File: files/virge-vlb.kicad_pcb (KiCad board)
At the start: 4 copper layers, 240.5 x 70.4 mm, 61 parts, among them J1 VLB_slot, J2 VGA, J3 VESA feature, U1 86C325, U10 74LS245, U2 27C010, Y1 14.318MHz

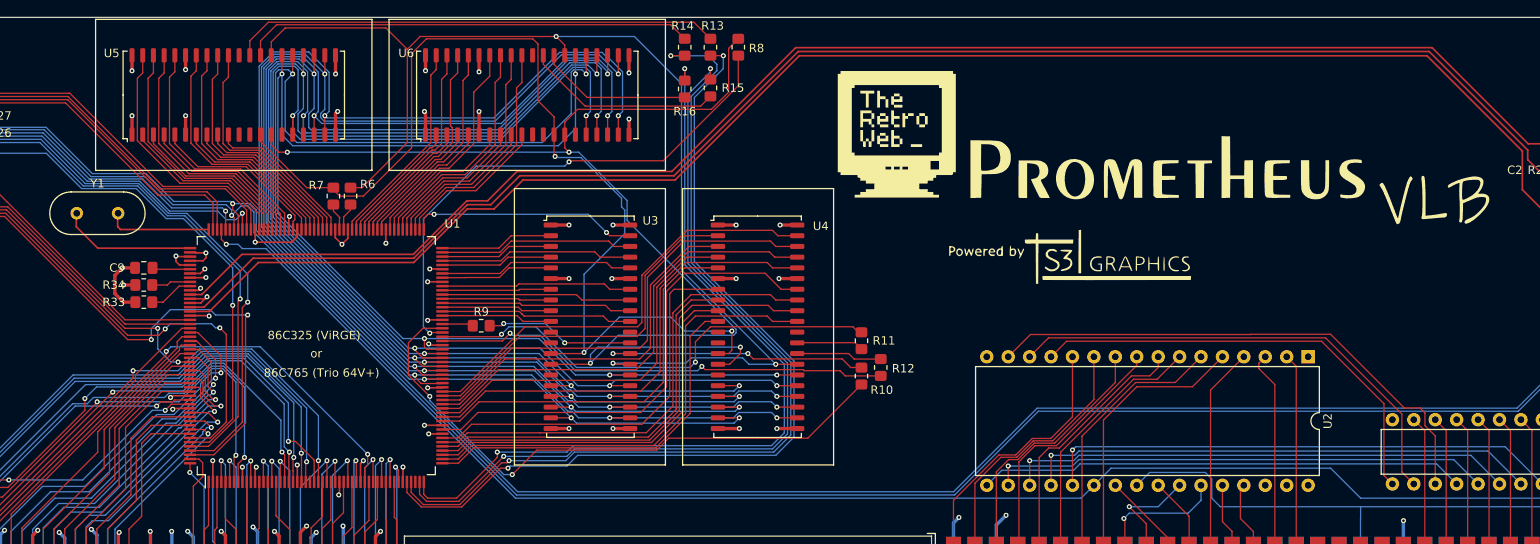
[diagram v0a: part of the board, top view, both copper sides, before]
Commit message: added register strap resistors
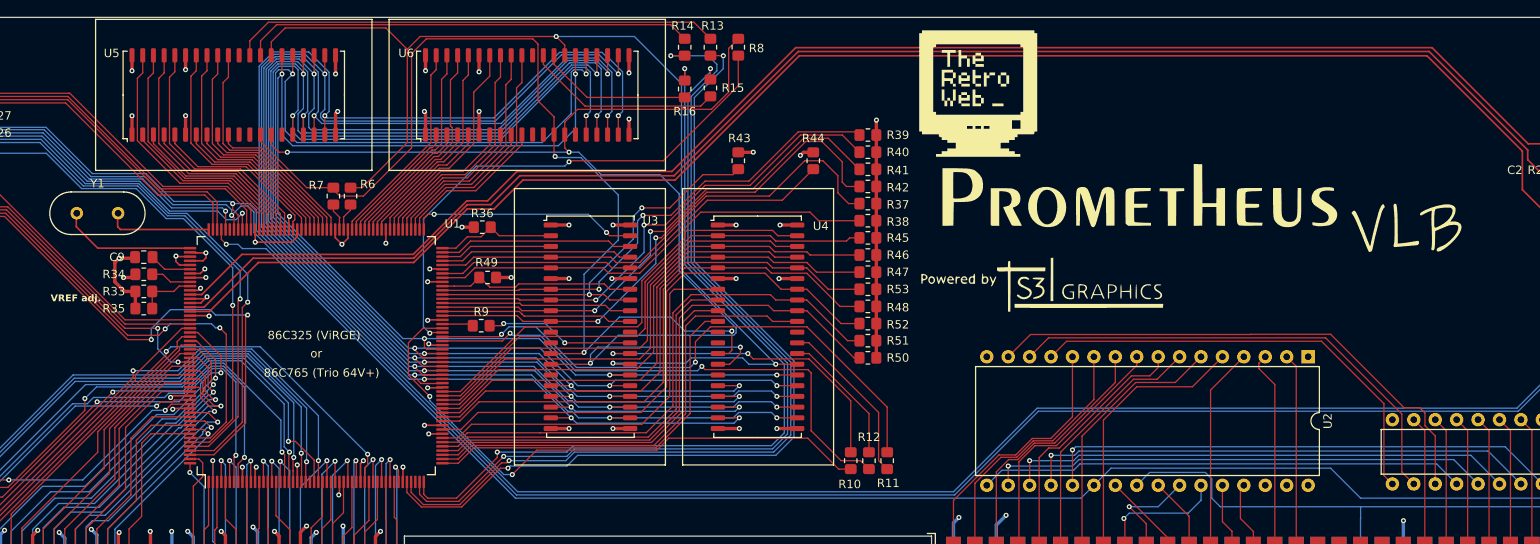
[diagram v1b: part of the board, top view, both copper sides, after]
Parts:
- added R35: ADJ, Resistor_SMD:R_0805_2012Metric_Pad1.20x1.40mm_HandSolder, F.Cu at (88.9, 111.1)
- added R36: 10K, Resistor_SMD:R_0805_2012Metric_Pad1.20x1.40mm_HandSolder, F.Cu at (129.0, 101.5)
- added R37: 10K, Resistor_SMD:R_0805_2012Metric_Pad1.20x1.40mm_HandSolder, F.Cu at (174.8, 98.7)
- added R38: 10K, Resistor_SMD:R_0805_2012Metric_Pad1.20x1.40mm_HandSolder, F.Cu at (174.8, 100.7)
- added R39: 10K, Resistor_SMD:R_0805_2012Metric_Pad1.20x1.40mm_HandSolder, F.Cu at (174.8, 90.6)
- added R40: 10K, Resistor_SMD:R_0805_2012Metric_Pad1.20x1.40mm_HandSolder, F.Cu at (174.8, 92.6)
- added R41: 10K, Resistor_SMD:R_0805_2012Metric_Pad1.20x1.40mm_HandSolder, F.Cu at (174.8, 94.6)
- added R42: 10K, Resistor_SMD:R_0805_2012Metric_Pad1.20x1.40mm_HandSolder, F.Cu at (174.8, 96.6)
- added R43: 10K, Resistor_SMD:R_0805_2012Metric_Pad1.20x1.40mm_HandSolder, F.Cu at (159.4, 93.6)
- added R44: 10K, Resistor_SMD:R_0805_2012Metric_Pad1.20x1.40mm_HandSolder, F.Cu at (168.3, 93.6)
- added R45: 10K, Resistor_SMD:R_0805_2012Metric_Pad1.20x1.40mm_HandSolder, F.Cu at (174.8, 102.7)
- added R46: 10K, Resistor_SMD:R_0805_2012Metric_Pad1.20x1.40mm_HandSolder, F.Cu at (174.8, 104.8)
- added R47: 10K, Resistor_SMD:R_0805_2012Metric_Pad1.20x1.40mm_HandSolder, F.Cu at (174.8, 106.8)
- added R48: 10K, Resistor_SMD:R_0805_2012Metric_Pad1.20x1.40mm_HandSolder, F.Cu at (174.8, 110.9)
- added R49: 10K, Resistor_SMD:R_0805_2012Metric_Pad1.20x1.40mm_HandSolder, F.Cu at (129.7, 107.4)
- added R50: 10K, Resistor_SMD:R_0805_2012Metric_Pad1.20x1.40mm_HandSolder, F.Cu at (174.8, 117.0)
- added R51: 10K, Resistor_SMD:R_0805_2012Metric_Pad1.20x1.40mm_HandSolder, F.Cu at (174.8, 114.9)
- added R52: 10K, Resistor_SMD:R_0805_2012Metric_Pad1.20x1.40mm_HandSolder, F.Cu at (174.8, 112.9)
- added R53: 10K, Resistor_SMD:R_0805_2012Metric_Pad1.20x1.40mm_HandSolder, F.Cu at (174.8, 108.8)
- moved R11 14.5 mm to (177.0, 129.2)
- moved R12 11.1 mm to (174.9, 129.2)
- moved G*** 10.8 mm to (187.8, 85.5)
- moved R10 10.1 mm to (172.7, 129.2)
- moved G*** 4.67 mm to (213.1, 102.7)
- moved C9 1.27 mm to (88.9, 105.0)
- moved R33 1.27 mm to (88.9, 109.1)
- moved R34 1.27 mm to (88.9, 107.1)
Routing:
- net /Memory Bus/PD7: track 13.1 -> 64.0 mm, vias 0 -> 2
- net /Memory Bus/PD6: track 13.0 -> 61.2 mm, vias 0 -> 2
- net /Memory Bus/PD5: track 12.9 -> 60.3 mm, vias 0 -> 2
- net /Memory Bus/PD4: track 12.9 -> 59.5 mm, vias 0 -> 2
- net /Memory Bus/PD2: track 13.2 -> 58.4 mm
- net /Memory Bus/PD3: track 13.3 -> 53.6 mm
- net GND: track 232.3 -> 269.2 mm, vias 48 -> 53
- net /Memory Bus/PD12: track 23.0 -> 49.6 mm
- net /Memory Bus/PD10: track 22.5 -> 48.7 mm, vias 0 -> 2
- net /Memory Bus/PD19: track 46.7 -> 65.3 mm
- net /Memory Bus/PD18: track 45.6 -> 63.1 mm
- net /Memory Bus/PD17: track 44.8 -> 62.0 mm
- net /Memory Bus/PD16: track 44.2 -> 61.0 mm
- net /Memory Bus/CAS2: track 7.94 -> 20.2 mm
- net Net-(U1F-~{CAS2}): track 55.9 -> 67.9 mm
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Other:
- board text added: "VREF adj."

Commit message: initial PCB routed
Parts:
- added C10: 0.1uF, Capacitor_SMD:C_0805_2012Metric_Pad1.18x1.45mm_HandSolder, F.Cu at (142.1, 132.2)
- added C11: 0.1uF, Capacitor_SMD:C_0805_2012Metric_Pad1.18x1.45mm_HandSolder, F.Cu at (161.8, 132.2)
- added C12: 0.1uF, Capacitor_SMD:C_0805_2012Metric_Pad1.18x1.45mm_HandSolder, F.Cu at (153.3, 80.1)
- added C13: 0.1uF, Capacitor_SMD:C_0805_2012Metric_Pad1.18x1.45mm_HandSolder, F.Cu at (80.4, 82.4)
- added C14: 0.1uF, Capacitor_SMD:C_0805_2012Metric_Pad1.18x1.45mm_HandSolder, F.Cu at (244.3, 131.8)
- added C15: 0.1uF, Capacitor_SMD:C_0805_2012Metric_Pad1.18x1.45mm_HandSolder, F.Cu at (62.7, 131.4)
- added R54: 0R, Resistor_SMD:R_0805_2012Metric_Pad1.20x1.40mm_HandSolder, F.Cu at (236.6, 134.2)
- added R55: 0R, Resistor_SMD:R_0805_2012Metric_Pad1.20x1.40mm_HandSolder, F.Cu at (244.5, 120.4)
- U10: footprint Package_DIP:DIP-20_W7.62mm -> Package_SO:SO-20_5.3x12.6mm_P1.27mm
- U2: value 27C010 -> 27C020
- moved R43 15.4 mm to (174.8, 93.7), turned to 180 degrees
- moved U2 13.0 mm to (239.9, 116.5)
- moved U10 8.05 mm to (251.8, 125.5), turned to 180 degrees
- moved G*** 7.98 mm to (221.0, 104.0)
- moved R44 6.75 mm to (174.8, 91.7), turned to 180 degrees
- moved R50 5.46 mm to (174.8, 122.4)
- moved R51 5.33 mm to (174.8, 120.3)
- moved R38 5.21 mm to (174.8, 105.9)
- moved R40 5.21 mm to (174.8, 97.8)
- moved R41 5.21 mm to (174.8, 99.8)
- moved R45 5.21 mm to (174.8, 108.0)
- moved R48 5.21 mm to (174.8, 116.1)
- moved R53 5.21 mm to (174.8, 114.0)
- moved R37 5.21 mm to (174.8, 103.9)
- moved R39 5.21 mm to (174.8, 95.8)
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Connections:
- J1 pad C4: /ISA Bus/IRQ2 -> unconnected-(J1B-IRQ2-PadC4)
- JP2 pad 1: /ISA Bus/IRQ2 -> unconnected-(JP2-Pin_1-Pad1)
- U2 pad 2: /ISA Bus/R_A16 -> Net-(U2-A16)
- U2 pad 30: (no net) -> Net-(U2-A17)
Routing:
- net GND: track 269.2 -> 337.4 mm, vias 53 -> 52
- net VCC: track 110.7 -> 160.7 mm, vias 36 -> 39
- net /ISA Bus/SMEMR: track 78.8 -> 49.0 mm, vias 0 -> 1
- net /ISA Bus/R_A16: track 25.6 -> 0.00 mm
- net /ISA Bus/R_D7: track 61.9 -> 38.9 mm, vias 1 -> 0
- net /Memory Bus/RAS: track 149.3 -> 129.4 mm
- net /ISA Bus/R_D6: track 61.1 -> 41.6 mm, vias 1 -> 0
- net /ISA Bus/R_D5: track 60.3 -> 43.8 mm, vias 1 -> 0
- net /ISA Bus/R_A5: track 32.6 -> 48.3 mm
- net /ISA Bus/R_A8: track 17.8 -> 33.0 mm, vias 1 -> 0
- net /ISA Bus/R_A3: track 32.5 -> 47.5 mm
- net /ISA Bus/R_A7: track 34.9 -> 49.8 mm
- net /ISA Bus/R_A4: track 33.0 -> 47.8 mm
- net /Memory Bus/PD10: track 48.7 -> 63.4 mm
- net /ISA Bus/R_A6: track 33.8 -> 48.2 mm
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
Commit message: added SAUP decoding, adjusted VGA conn.
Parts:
- removed J3: VESA feature, Connector_PinHeader_2.54mm:PinHeader_2x13_P2.54mm_Vertical
- removed JP2: IRQ select, Connector_PinHeader_2.54mm:PinHeader_1x03_P2.54mm_Vertical
- removed R22, R23, R24, R25, R26, R28, R30, R32: 33R, Resistor_SMD:R_0805_2012Metric_Pad1.20x1.40mm_HandSolder
- removed R27, R29, R31: 4K7, Resistor_SMD:R_0805_2012Metric_Pad1.20x1.40mm_HandSolder
- added C16: 0.1uF, Capacitor_SMD:C_0805_2012Metric_Pad1.18x1.45mm_HandSolder, F.Cu at (88.4, 115.4)
- added C17: 0.1uF, Capacitor_SMD:C_0805_2012Metric_Pad1.18x1.45mm_HandSolder, F.Cu at (84.1, 115.4)
- added C18: 0.1uF, Capacitor_SMD:C_0805_2012Metric_Pad1.18x1.45mm_HandSolder, F.Cu at (86.2, 115.4)
- added U7: 74LS244, Package_SO:SO-20_5.3x12.6mm_P1.27mm, F.Cu at (253.6, 125.5)
- added U8: 4052, Package_SO:SO-16_3.9x9.9mm_P1.27mm, F.Cu at (77.6, 113.5)
- added U9: 74HC04, Package_SO:SO-14_3.9x8.65mm_P1.27mm, F.Cu at (59.4, 118.0)
- R18, R19, R20: value 33R -> 10K
- R21: value 33R -> 4K7
- U10: value 74LS245 -> 7408; footprint Package_SO:SO-20_5.3x12.6mm_P1.27mm -> Package_SO:SO-14_3.9x8.65mm_P1.27mm
- moved U10 193.1 mm to (59.4, 109.1), turned to 90 degrees
- moved R18 33.9 mm to (73.4, 108.0), turned to 0 degrees
- moved R19 32.0 mm to (66.8, 111.6), turned to 90 degrees
- moved R20 30.6 mm to (69.0, 111.6), turned to -90 degrees
- moved R21 29.4 mm to (71.1, 111.6), turned to -90 degrees
- moved C3 11.7 mm to (258.8, 87.4), turned to 0 degrees
- moved C1 11.3 mm to (267.0, 87.4), turned to 0 degrees
- moved C7 11.1 mm to (267.2, 119.9)
- moved C8 11.1 mm to (267.2, 117.3)
- moved R4 11.1 mm to (267.2, 122.0)
- moved R5 11.1 mm to (267.2, 115.2)
- moved C2 9.92 mm to (263.0, 87.4), turned to 0 degrees
- moved R3 9.11 mm to (258.8, 89.7), turned to 0 degrees
- moved R1 8.64 mm to (267.0, 89.7), turned to 0 degrees
- moved J2 8.21 mm to (274.7, 101.2)
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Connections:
- J1 pad A22: /VL Bus/VL_A28 -> unconnected-(J1A-A28-PadA22)
- J1 pad A54: /VL Bus/ID2 -> unconnected-(J1A-ID2-PadA54)
- J1 pad A55: /VL Bus/ID3 -> unconnected-(J1A-ID3-PadA55)
- J1 pad A56: /VL Bus/ID4 -> unconnected-(J1A-ID4-PadA56)
- J1 pad B21: /VL Bus/VL_A31 -> unconnected-(J1A-A31-PadB21)
- J1 pad B24: /VL Bus/VL_A27 -> unconnected-(J1A-A27-PadB24)
- J1 pad B53: /VL Bus/ID0 -> unconnected-(J1A-ID0-PadB53)
- J1 pad B54: /VL Bus/ID1 -> unconnected-(J1A-ID1-PadB54)
- J1 pad C46: /ISA Bus/R_A16 -> unconnected-(J1B-BA16-PadC46)
- J2 pad 12: unconnected-(J2-Pad12) -> Net-(U8-Y3)
- J2 pad 15: unconnected-(J2-Pad15) -> Net-(U8-X3)
- R18 pad 1: Net-(U1D-LD0/PA0) -> VCC
- R19 pad 1: Net-(U1D-LD1/PA1) -> Net-(U8-Y1)
- R19 pad 2: Net-(J3-Pin_4) -> VCC
- R20 pad 1: Net-(U1D-LD2/PA2) -> VCC
- R20 pad 2: Net-(J3-Pin_6) -> Net-(U8-Y3)
- R21 pad 1: Net-(U1D-LD3/PA3) -> VCC
- R21 pad 2: Net-(J3-Pin_8) -> Net-(U8-X3)
- U1 pad 146: Net-(U1D-LD0/PA0) -> unconnected-(U1D-LD0/PA0-Pad146)
- U1 pad 147: Net-(U1D-LD1/PA1) -> unconnected-(U1D-LD1/PA1-Pad147)
- U1 pad 148: /LCLK -> unconnected-(U1H-LCLK/VCLK-Pad148)
- U1 pad 151: unconnected-(U1H-~{GPIOSTR}/~{ENFEAT}/GOP0-Pad151) -> /ENFEAT
- U1 pad 152: /VL Bus/SINTR -> /VL Bus/IRQ9
- U1 pad 154: Net-(U1D-LD2/PA2) -> unconnected-(U1D-LD2/PA2-Pad154)
- U1 pad 155: Net-(U1D-LD3/PA3) -> unconnected-(U1D-LD3/PA3-Pad155)
- U1 pad 174: Net-(U1D-LD4/PA4) -> unconnected-(U1D-LD4/PA4-Pad174)
- U1 pad 175: Net-(U1D-LD5/PA5) -> unconnected-(U1D-LD5/PA5-Pad175)
- U1 pad 184: Net-(U1D-LD6/PA6) -> unconnected-(U1D-LD6/PA6-Pad184)
- U1 pad 202: Net-(U1D-LD7/PA7) -> unconnected-(U1D-LD7/PA7-Pad202)
- U1 pad 203: /EVIDEO -> unconnected-(U1H-~{VREQ}/VRDY/EVIDEO-Pad203)
- U1 pad 204: /EVCLK -> unconnected-(U1H-~{CREQ}/CRDY/EVCLK-Pad204)
- U1 pad 205: /ESYNC -> /SPCLK
- U1 pad 206: /BLANK -> /SPD
- U1 pad 25: unconnected-(U1H-SAUP1-Pad25) -> /VL Bus/SAUP1
- U1 pad 50: unconnected-(U1H-SAUP2-Pad50) -> /VL Bus/VL_A30
- U10 pad 1: /ISA Bus/SMEMR -> Net-(U10-Pad1)
- U10 pad 10: GND -> Net-(U10-Pad10)
- U10 pad 11: /ISA Bus/R_D0 -> /VL Bus/SAUP1
- U10 pad 12: /ISA Bus/R_D1 -> Net-(U10-Pad12)
- U10 pad 13: /ISA Bus/R_D2 -> Net-(U10-Pad13)
- U10 pad 14: /ISA Bus/R_D3 -> VCC
- U10 pad 2: /ISA Bus/ISA_D7 -> Net-(U10-Pad2)
- U10 pad 3: /ISA Bus/ISA_D6 -> Net-(U10-Pad3)
- U10 pad 4: /ISA Bus/ISA_D5 -> Net-(U10-Pad4)
- U10 pad 5: /ISA Bus/ISA_D4 -> Net-(U10-Pad5)
- U10 pad 6: /ISA Bus/ISA_D3 -> Net-(U10-Pad10)
- U10 pad 7: /ISA Bus/ISA_D2 -> GND
- U10 pad 8: /ISA Bus/ISA_D1 -> Net-(U10-Pad12)
- U10 pad 9: /ISA Bus/ISA_D0 -> Net-(U10-Pad3)
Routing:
- net Net-(U8-Y3): track 0.00 -> 288.1 mm, vias 0 -> 1
- net Net-(U8-X3): track 0.00 -> 268.8 mm, vias 0 -> 1
- net GND: track 337.4 -> 176.2 mm, vias 52 -> 53
- net /VL Bus/VL_A23: track 0.00 -> 90.4 mm, vias 0 -> 3
- net /VL Bus/VL_A24: track 0.00 -> 89.2 mm, vias 0 -> 4
- net /VL Bus/VL_A29: track 0.00 -> 88.5 mm, vias 0 -> 3
- net /VL Bus/VL_A26: track 0.00 -> 86.6 mm, vias 0 -> 4
- net /VL Bus/VL_A25: track 0.00 -> 85.5 mm, vias 0 -> 3
- net /BLANK: track 85.3 -> 0.00 mm, vias 2 -> 0
- net /EVCLK: track 80.3 -> 0.00 mm, vias 2 -> 0
- net /VL Bus/SINTR: track 74.1 -> 0.00 mm, vias 1 -> 0
- net /VL Bus/SAUP1: track 0.00 -> 73.5 mm, vias 0 -> 2
- net /ESYNC: track 69.9 -> 0.00 mm, vias 2 -> 0
- net /VS: track 260.9 -> 194.3 mm
- net Net-(U1D-LD7/PA7): track 65.9 -> 0.00 mm, vias 2 -> 0
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- added copper zone on F.Cu, net GND
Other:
- board text added: "74LS244"
- board text added: "Bank 0"
- board text added: "Bank 1"
- board text added: "S3 chip goes here lol"
- board text added: "Video BIOS"
- board text removed: "86C325 (ViRGE)"
- board text removed: "86C765 (Trio 64V+)"
- board text removed: "or"

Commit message: added ground vias, polished silkscreen
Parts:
- C10, C11, C12, C13, C14, C15, C9: value 0.1uF -> 100nF
- C17: value 0.1uF -> 3 x 100nF
- C3, C6: value 10pF -> 3 x 10pF
- R10, R13: value 33R -> 3 x 33R
- R16, R6: value 33R -> 2 x 33R
- R3: value 75R -> 3 x 75R
- R44: value 10K -> 10K each
- R54, R55: value 0R -> 0
- U9: value 74HC04 -> 7404
- moved R18 0.90 mm to (74.3, 108.1)
- moved C7 0.27 mm to (267.0, 119.9)
- moved R4 0.25 mm to (267.0, 122.0)
- moved C8 0.24 mm to (267.0, 117.3)
- moved R5 0.24 mm to (267.0, 115.2)
- renumbered J2 to VGA
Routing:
- net GND: track 176.2 -> 171.7 mm, vias 53 -> 160
- net VCC: track 171.7 -> 174.0 mm
- net /VL Bus/SAUP1: track 73.5 -> 72.3 mm
- added copper zone on B.Cu, net GND
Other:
- board text added: "Config section"
- board text added: "Very Long Bus"
- board text added: "more Config"

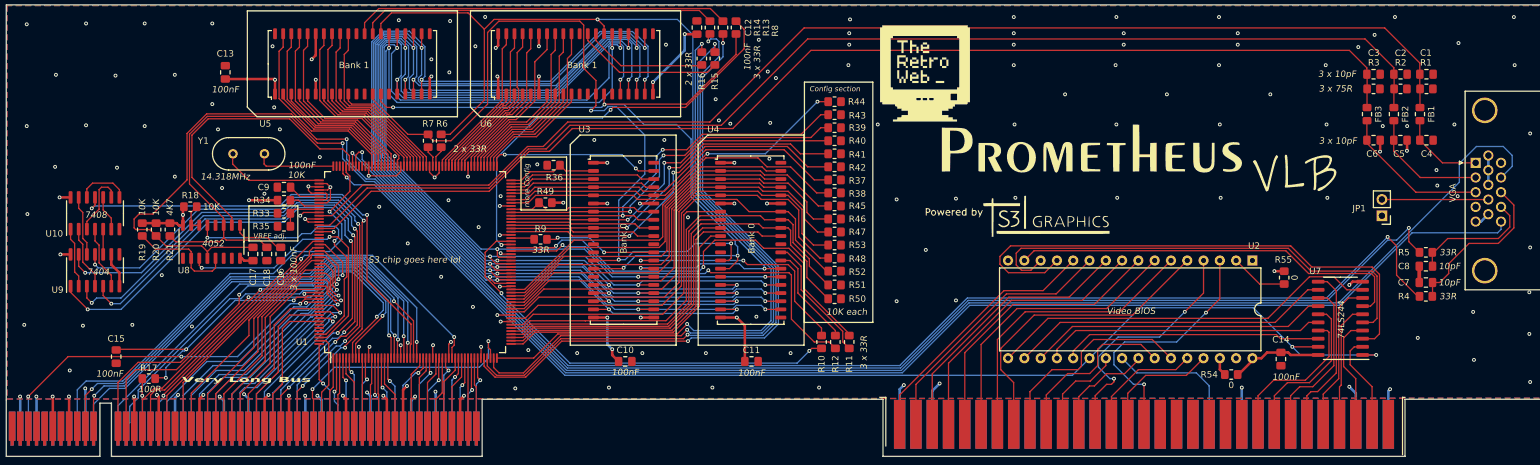
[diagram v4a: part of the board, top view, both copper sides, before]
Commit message: added address jumpers
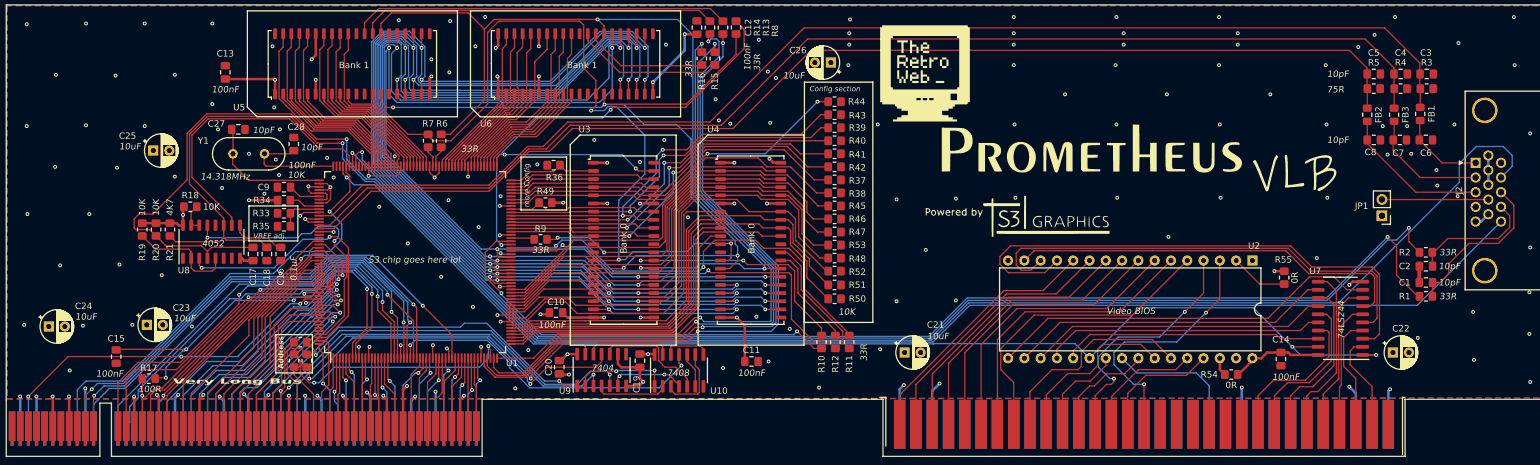
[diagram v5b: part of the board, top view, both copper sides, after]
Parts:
- removed VGA: VGA, Connector_Dsub:DSUB-15-HD_Female_Horizontal_P2.29x1.98mm_EdgePinOffset8.35mm_Housed_MountingHolesOffset10.89mm
- added C10: 100nF, Capacitor_SMD:C_0805_2012Metric_Pad1.18x1.45mm_HandSolder, F.Cu at (131.3, 124.6)
- added C20: 100nF, Capacitor_SMD:C_0805_2012Metric_Pad1.18x1.45mm_HandSolder, F.Cu at (131.8, 133.1)
- added C21: 10uF, Capacitor_THT:CP_Radial_D5.0mm_P2.50mm, F.Cu at (185.7, 130.8)
- added C22: 10uF, Capacitor_THT:CP_Radial_D5.0mm_P2.50mm, F.Cu at (261.8, 130.8)
- added C23: 10uF, Capacitor_THT:CP_Radial_D5.0mm_P2.50mm, F.Cu at (67.5, 126.5)
- added C24: 10uF, Capacitor_THT:CP_Radial_D5.0mm_P2.50mm, F.Cu at (52.2, 126.7)
- added C25: 10uF, Capacitor_THT:CP_Radial_D5.0mm_P2.50mm, F.Cu at (68.5, 99.3)
- added C26: 10uF, Capacitor_THT:CP_Radial_D5.0mm_P2.50mm, F.Cu at (174.2, 85.6)
- added C27: 10pF, Capacitor_SMD:C_0805_2012Metric_Pad1.18x1.45mm_HandSolder, F.Cu at (81.8, 96.0)
- added C28: 10pF, Capacitor_SMD:C_0805_2012Metric_Pad1.18x1.45mm_HandSolder, F.Cu at (90.4, 98.3)
- added J2: VGA, Connector_Dsub:DSUB-15-HD_Female_Horizontal_P2.29x1.98mm_EdgePinOffset8.35mm_Housed_MountingHolesOffset10.89mm, F.Cu at (274.7, 101.2)
- added R22: 0, Resistor_SMD:R_0805_2012Metric_Pad1.20x1.40mm_HandSolder, F.Cu at (91.4, 129.2)
- added R23: 0, Resistor_SMD:R_0805_2012Metric_Pad1.20x1.40mm_HandSolder, F.Cu at (92.5, 132.1)
- added R24: 0, Resistor_SMD:R_0805_2012Metric_Pad1.20x1.40mm_HandSolder, F.Cu at (90.5, 132.1)
- C17: value 3 x 100nF -> 0.1uF
- C3, C6: value 3 x 10pF -> 10pF
- R1, R2: value 75R -> 33R
- R10, R13: value 3 x 33R -> 33R
- R16, R6: value 2 x 33R -> 33R
- R3: value 3 x 75R -> 75R
- R4, R5: value 33R -> 75R
- R44: value 10K each -> 10K
- R54, R55: value 0 -> 0R
- moved U10 94.3 mm to (150.5, 133.6)
- moved U9 80.5 mm to (138.4, 133.5)
- moved R4 32.6 mm to (263.0, 89.7)
- moved C1 32.5 mm to (267.0, 119.9), turned to 180 degrees
- moved R1 32.3 mm to (267.0, 122.0)
- moved C2 30.2 mm to (267.0, 117.3), turned to 180 degrees
- moved R5 26.8 mm to (258.8, 89.7)
- moved R2 25.8 mm to (267.0, 115.2)
- moved C7 22.6 mm to (262.9, 97.7)
- moved C8 21.3 mm to (258.8, 97.7)
- moved C5 11.1 mm to (258.8, 87.4)
- moved C4 11.1 mm to (263.0, 87.4)
- moved C3 8.29 mm to (267.1, 87.4)
- moved R3 8.29 mm to (267.1, 89.7)
- moved C6 8.17 mm to (267.0, 97.7)
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- renumbered C10 to C19
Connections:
- net Net-(U8-X3) renamed /DDC_SCL
- net Net-(U8-Y3) renamed /DDC_SDA
- C1 pad 1: /S3_RED -> Net-(C1-Pad1)
- C2 pad 1: /S3_GREEN -> Net-(C2-Pad1)
- C3 pad 1: /S3_BLUE -> /S3_RED
- C4 pad 1: /RED -> /S3_GREEN
- C5 pad 1: /GREEN -> /S3_BLUE
- C6 pad 1: /BLUE -> /RED
- C7 pad 1: GND -> /GREEN
- C7 pad 2: /HSYNC -> GND
- C8 pad 1: GND -> /BLUE
- C8 pad 2: /VSYNC -> GND
- FB2 pad 1: /GREEN -> /BLUE
- FB2 pad 2: /S3_GREEN -> /S3_BLUE
- FB3 pad 1: /BLUE -> /GREEN
- FB3 pad 2: /S3_BLUE -> /S3_GREEN
- R1 pad 1: /S3_RED -> /HS
- R1 pad 2: GND -> Net-(C1-Pad1)
- R2 pad 1: /S3_GREEN -> /VS
- R2 pad 2: GND -> Net-(C2-Pad1)
- R3 pad 1: /S3_BLUE -> /S3_RED
- R4 pad 1: /HS -> /S3_GREEN
- R4 pad 2: /HSYNC -> GND
- R5 pad 1: /VS -> /S3_BLUE
- R5 pad 2: /VSYNC -> GND
- U1 pad 50: /VL Bus/VL_A30 -> /VL Bus/SAUP2
- U9 pad 11: /VL Bus/VL_A26 -> Net-(R23-Pad1)
- U9 pad 5: /VL Bus/VL_A25 -> Net-(R22-Pad1)
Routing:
- net /VL Bus/VL_A25: track 85.5 -> 14.1 mm, vias 3 -> 1
- net /VL Bus/VL_A26: track 86.5 -> 16.0 mm, vias 4 -> 0
- net Net-(R22-Pad1): track 0.00 -> 56.3 mm, vias 0 -> 2
- net Net-(R23-Pad1): track 0.00 -> 56.0 mm, vias 0 -> 2
- net /VL Bus/SAUP2: track 0.00 -> 38.9 mm, vias 0 -> 2
- net /VL Bus/VL_A30: track 40.7 -> 10.5 mm, vias 2 -> 0
- net /VL Bus/VL_A23: track 90.4 -> 61.2 mm, vias 3 -> 1
- net /VL Bus/VL_A29: track 88.5 -> 61.1 mm, vias 3 -> 1
- net /VL Bus/VL_A24: track 89.2 -> 63.3 mm, vias 4 -> 2
- net Net-(C1-Pad1): track 0.00 -> 25.7 mm
- net /HSYNC: track 25.7 -> 0.00 mm
- net /VL Bus/SAUP1: track 72.3 -> 51.6 mm
- net /VSYNC: track 19.6 -> 0.00 mm
- net Net-(C2-Pad1): track 0.00 -> 19.4 mm
- net Net-(U10-Pad5): track 3.94 -> 17.5 mm
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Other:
- board text added: "1GB"
- board text added: "32MB"
- board text added: "64MB"
- board text added: "Address"
- board text added: "Address location:"
